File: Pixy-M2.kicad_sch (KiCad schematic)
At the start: 78 parts, among them J1 USB_C_Receptacle_USB2.0_14P, J10 SM09B-SRSS-TB, J11 SM06B-SRSS-TB, J4 SM06B-SRSS-TB, J5 SM06B-SRSS-TB, J6 SM06B-SRSS-TB, J7 SM06B-SRSS-TB, J8 SM06B-SRSS-TB, J9 SM06B-SRSS-TB, Q1 AO4407A, SW1 SW_Push, SW2 SW_Push, SW3 JS102011SAQN, U1 ESP32-S3-WROOM-1-N16, U2 USBLC6-2SC6, U3 AP63203WU, U4 DRV8231ADSG, U5 DRV8231ADSG

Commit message: layout: replace F1 with a fuse that breaks the pack's short-circuit current
The chosen pack (OVONIC 2S 450 mAh 100C, XT30) is estimated to put 200-400 A
into a dead short (8-15 mOhm/cell plus connectors, lead, fuse and copper; Ovonic
publishes no internal resistance). The 2920L300/15DR PPTC was rated to break
40 A. A lower-C pack was rejected to keep burst current for the motors, and the
451/453 NANO2 parts (300-400 A @ 32 VDC) sit inside the estimate.

F1 is now a Littelfuse 0885005.DR: 5 A fast-acting, 1500 A @ 125 VDC breaking,
11.9 mOhm. 5 A covers the ~2.4 A worst normal load (both motors at the 1.00 A
limit plus the buck) after the 25% derating. It is one-time: jams are handled
by the drivers' current limit and firmware stall detection. Symbol goes
Device:Polyfuse -> Device:Fuse (same pins); F2 stays a PPTC. Netlist diff:
only F1's value and footprint. ERC 0.

Board: new last routing stage, tools/autoroute/f1_fuse.py. The 16.1 x 7.3 mm
land pattern sits at (110.2, 100.7) between BT1 and Q1; its 7.76 mm courtyard
did not fit the 7.65 mm BT1-D6 gap, so BT1 moves 0.4 mm north (J6 still 2.6 mm
away; verify_placement.py: no underside clashes). /VBAT_RAW and /VBAT_FUSED
re-routed at 1.0 mm; no other net changed. D6's reference moved off F1 pad 2.
DRC: 0 violations, 0 unconnected, 0 parity. Aperture audit passes.

pololu_conn.py fixes found on the way, with J8/J9 copper unchanged:
_zone() uses pad extents rather than centres, and dangling() counts a track
end whose copper overlaps a pad or via as connected.

Co-Authored-By: Claude Opus 5.5 <noreply@anthropic.com>
Claude-Session: https://claude.ai/code/session_01MLrob72MX5PcwtzVMbc3bs
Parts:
- F1: value 3A 15V -> 5A 1500A@125VDC; footprint Fuse:Fuse_2920_7451Metric -> Fuse:Fuse_Littelfuse-NANO2-885; symbol Device:Polyfuse -> Device:Fuse; MPN 2920L300/15DR -> 0885005.DR
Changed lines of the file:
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@@
 	)
 	(symbol
-		(lib_id "Device:Polyfuse")
+		(lib_id "Device:Fuse")
 		(at 161.29 73.66 90)
 		(unit 1)
@@
 			)
 		)
-		(property "Value" "3A 15V"
+		(property "Value" "5A 1500A@125VDC"
 			(at 161.29 68.58 90)
 			(effects
@@
 			)
 		)
-		(property "Footprint" "Fuse:Fuse_2920_7451Metric"
+		(property "Footprint" "Fuse:Fuse_Littelfuse-NANO2-885"
 			(at 161.29 73.66 0)
 			(hide yes)
@@
 			)
 		)
-		(property "Datasheet" "https://www.littelfuse.com/assetdocs/2920l_datasheet_update.pdf?assetguid=f237e8c2-1ed9-4c13-a738-dbe0738b3d2c"
+		(property "Datasheet" "https://www.littelfuse.com/assetdocs/littelfuse-fuse-885-datasheet?assetguid=f4426cf6-2a53-41b3-b8da-211f7a44fad1"
 			(at 161.29 73.66 0)
 			(hide yes)
@@
 			)
 		)
-		(property "Description" "Battery PPTC: 3A hold / 5A trip at 20C, 15V, 40A maximum fault current. Provisional; verify motor/fan load and pack fault current."
+		(property "Description" "Battery fuse, one-time: Littelfuse 885 series 5A, breaks 1500A @ 125VDC. Sized for the pack short-circuit current (OVONIC 2S 450mAh 100C, est. 200-400A); the old 2920 PPTC was rated for 40A max fault. 200% opens in 2 min max; max normal load ~2.4A."
 			(at 161.29 73.66 0)
 			(hide yes)
@@
 			)
 		)
-		(property "MPN" "2920L300/15DR"
+		(property "MPN" "0885005.DR"
 			(at 161.29 73.66 0)
 			(hide yes)

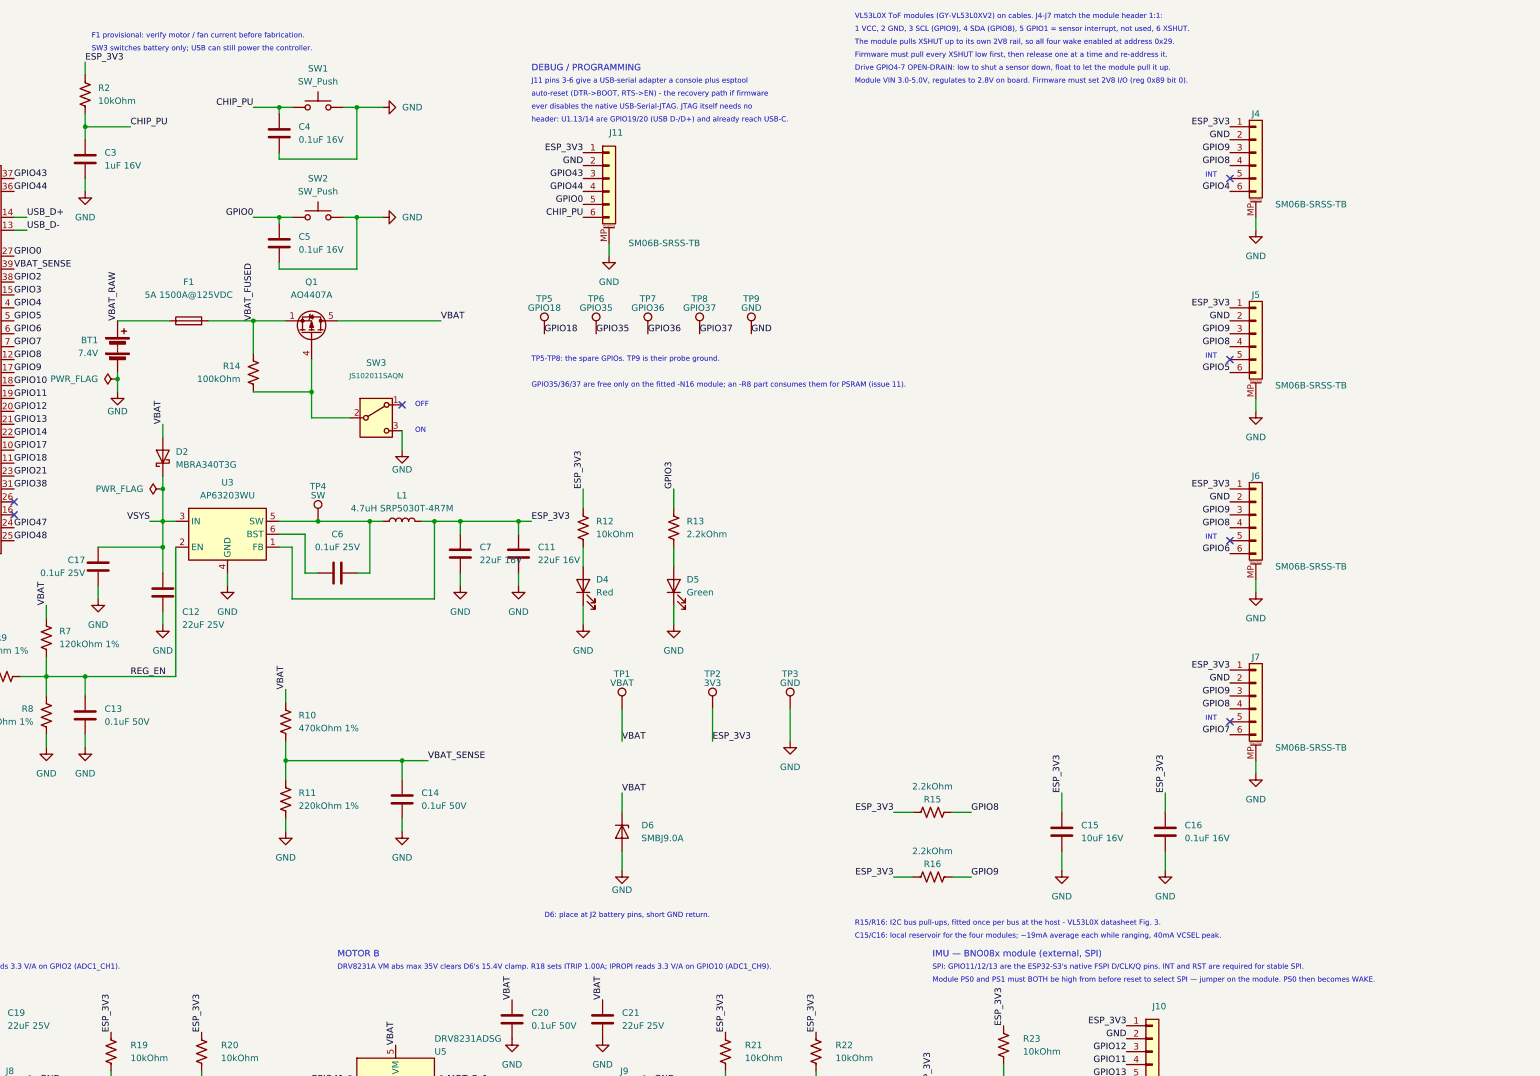
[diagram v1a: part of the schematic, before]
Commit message: schematic: correct three stale sheet notes
- F1 is no longer provisional: it is the 0885005.DR one-time fuse, sized
  to break the pack's short-circuit current, and there is no fan.
- D6 goes beside the motor drivers; J2 was deleted on 2026-09-20.
- The IMU note implied both PS0 and PS1 are module jumpers. Only PS1 is;
  PS0 is WAKE on GPIO17, held high by firmware while RST is pulsed.

Text only: the netlist is byte-identical and ERC is 0. The README's
schematic render is regenerated to match.

Co-Authored-By: Claude Opus 5.5 <noreply@anthropic.com>
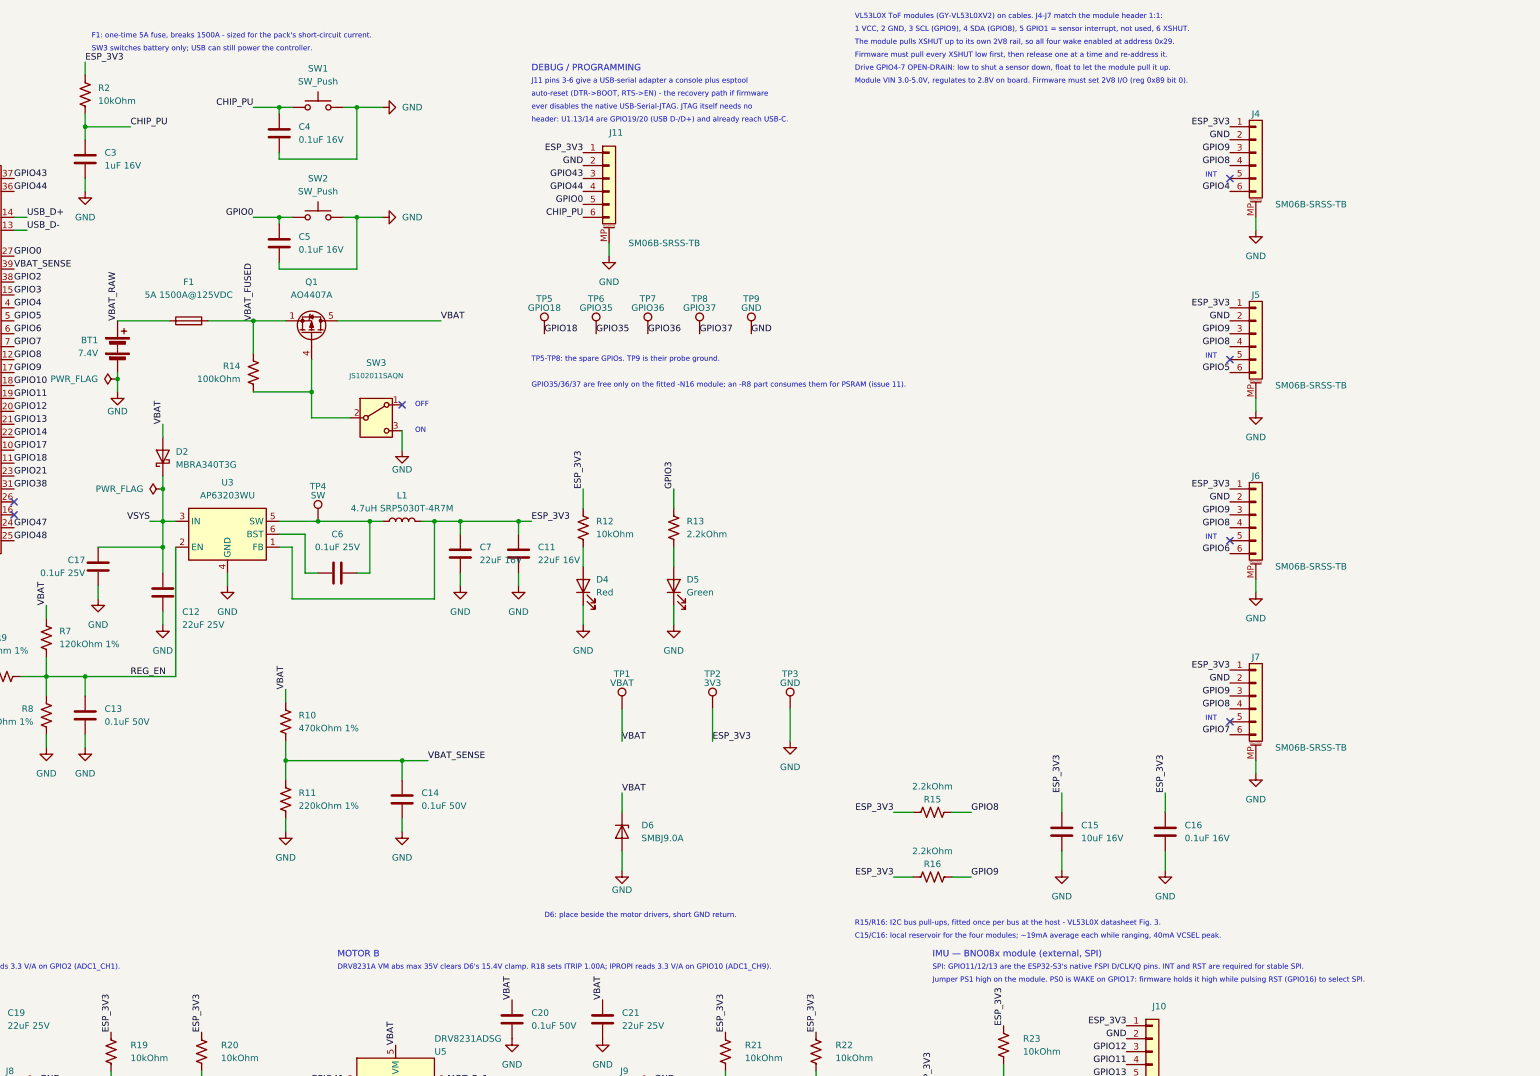
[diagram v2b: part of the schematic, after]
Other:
- note added: "D6: place beside the motor drivers, short GND return."
- note added: "F1: one-time 5A fuse, breaks 1500A - sized for the pack's short-circuit current."
- note added: "Jumper PS1 high on the module. PS0 is WAKE on GPIO17: firmware holds it high while pulsing RST (GPIO16) to select SPI."
- note removed: "D6: place at J2 battery pins, short GND return."
- note removed: "F1 provisional: verify motor / fan current before fabrication."
- note removed: "Module PS0 and PS1 must BOTH be high from before reset to select SPI — jumper on the module. PS0 then becomes WAKE."
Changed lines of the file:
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@@
 		)
 	)
-	(text "F1 provisional: verify motor / fan current before fabrication."
+	(text "F1: one-time 5A fuse, breaks 1500A - sized for the pack's short-circuit current."
 		(at 142.24 17.78 0)
 		(effects
@@
 		)
 	)
-	(text "D6: place at J2 battery pins, short GND return."
+	(text "D6: place beside the motor drivers, short GND return."
 		(at 231.14 190.5 0)
 		(effects
@@
 		)
 	)
-	(text "Module PS0 and PS1 must BOTH be high from before reset to select SPI — jumper on the module. PS0 then becomes WAKE."
+	(text "Jumper PS1 high on the module. PS0 is WAKE on GPIO17: firmware holds it high while pulsing RST (GPIO16) to select SPI."
 		(at 307.34 203.2 0)
 		(effects

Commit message: schematic: re-lay out the sheet into framed blocks
Layout only. Every wire-connected cluster moved rigidly into one of 13
dashed, titled frames in three rows: MCU, reset/boot, indicators/test
points, debug, battery sense, ToF; USB-C, battery input, 3V3 buck, UVLO;
motor A, motor B, IMU. The empty bottom band and right-centre of the A3
sheet are now used.

Two blocks were redrawn inside:
- USB: the CC resistors drop to GND without crossing D+/D-, the pair
  steps down to a lowered U2, and U2 takes VBUS by label.
- UVLO: the divider reaches U3.2 through its existing REG_EN label
  instead of a wire under the buck, so the blocks can sit apart.

Also fixed text overlaps: C1/C2, C7/C11, C8/R5 and C12. Long notes are
re-wrapped; their wording is unchanged.

Verified: netlist diff 0 differences (66 nets, 78 parts), ERC 0/0, PCB
DRC with schematic parity 0 violations / 0 unconnected / 0 parity. The
scripts are in tools/schematic, with netdiff.py for future edits.

Co-Authored-By: Claude Opus 5.5 <noreply@anthropic.com>
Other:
- note added: "3V3 BUCK — AP63203"
- note added: "BATTERY INPUT / POWER SWITCH"
- note added: "BATTERY SENSE"
- note added: "INDICATORS / TEST POINTS"
- note added: "MCU — ESP32-S3-WROOM-1-N16"
- note added: "RESET / BOOT"
- note added: "TOF WALL SENSORS — 4× VL53L0X"
- note added: "USB-C INPUT"
- note added: "UVLO — REGULATOR ENABLE"
- moved on the sheet: BT1, C1, C11, C12, C13, C14, C15, C16, C17, C18, C19, C2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

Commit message: U1: plug-in ESP32-S3-DevKitC-1-N8R8 on SMD sockets, same 66 x 100 mm board
Replace the soldered WROOM-1 module with an Espressif ESP32-S3-DevKitC-1-N8R8
(v1.1) on two 1x22 2.54 mm SMD female headers, and remove what the devkit
carries itself. The outline stays 66 x 100 mm for the diagonal runs.

Schematic (tools/schematic/devkit.py):
- U1 -> PCM_Espressif:ESP32-S3-DevKitC on Pixy-M2:ESP32-S3-DevKitC-1_SMD_Sockets;
  Value, Footprint, Datasheet and MPN changed together.
- 21 parts removed: the USB-C input (J1, U2, F2, R1, R5, R6, C8), the USB
  supply path (D1, D3, R9), reset/boot (R2, C3-C5, SW1, SW2), J11 and TP5-TP8.
- The AP63203 feeds the devkit's 3V3 pins; its 5V pin is unused.
- Encoder B OUT B moves from GPIO38 (the v1.1 RGB LED) to GPIO18.
- 13 no-connect flags on the pins the devkit uses itself. 59 nets, 57 parts,
  ERC 0/0.

Layout (tools/autoroute/devkit.py, new rework stage 20):
- U1 along the right edge, antenna over the rear edge, USB end to the front.
- The IMU moves into the 25 mm column beside the devkit (8.6 mm left of and
  7.5 mm behind the rotation centre). J10/C22 go behind it, J8/SW3 clear of
  it, J9 in front of the devkit, the LEDs to the rear-left corner and the
  sense chain against GPIO1.
- Rips and re-routes every affected net, keeping the hand-placed motor-corner,
  buck, FB and REG_EN copper. A* respects the custom clearance floors. The
  stage ends with KiCad-style dead-end pruning, removal of via-only GND stubs
  and one GND via per B.Cu pour island.
- Closes J1's outline notch and moves the antenna keep-out.
- Footprint generator: tools/autoroute/devkit_footprint.py.
- DRC 0 violations / 0 unconnected / 0 parity. Aperture audit passes with
  192 vias (254 on main). A full rework.py replay reproduces the board.
- Measurements are in layout/devkit/. Motor loops: A 26.4 mm², B 27.8 mm²
  (main 23.9 / 9.8, where B's opposite lobes nearly cancelled).

Rules: USB rules and netclass removed; Hole clearance 0.30 mm everywhere.
via_openings.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
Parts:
- removed C3: 1uF 16V, Capacitor_SMD:C_0603_1608Metric, symbol Device:C
- removed C4, C5: 0.1uF 16V, Capacitor_SMD:C_0603_1608Metric, symbol Device:C
- removed C8: 4.7nF 1kV, Capacitor_SMD:C_1206_3216Metric, symbol Device:C
- removed D1: MBRA340T3G, Diode_SMD:D_SMA, symbol Device:D_Schottky
- removed D3: BAT54W, Diode_SMD:D_SOD-123, symbol Device:D_Schottky
- removed F2: 500mA 15V, Fuse:Fuse_1812_4532Metric, symbol Device:Polyfuse
- removed J1: USB_C_Receptacle_USB2.0_14P, Connector_USB:USB_C_Receptacle_Amphenol_12401948E412A, symbol Connector:USB_C_Receptacle_USB2.0_14P
- removed J11: SM06B-SRSS-TB, Connector_JST:JST_SH_SM06B-SRSS-TB_1x06-1MP_P1.00mm_Horizontal, symbol Connector_Generic_MountingPin:Conn_01x06_MountingPin
- removed R1, R6: 5.1kOhm, Resistor_SMD:R_0805_2012Metric, symbol Device:R_US
- removed R2: 10kOhm, Resistor_SMD:R_0805_2012Metric, symbol Device:R_US
- removed R5: 1MOhm, Resistor_SMD:R_0805_2012Metric, symbol Device:R_US
- removed R9: 39kOhm 1%, Resistor_SMD:R_0805_2012Metric, symbol Device:R_US
- removed SW1, SW2: SW_Push, Button_Switch_SMD:SW_Push_1P1T_NO_E-Switch_TL3301NxxxxxG, symbol Switch:SW_Push
- removed TP5: GPIO18, TestPoint:TestPoint_Pad_D1.5mm, symbol Connector:TestPoint
- removed TP6: GPIO35, TestPoint:TestPoint_Pad_D1.5mm, symbol Connector:TestPoint
- removed TP7: GPIO36, TestPoint:TestPoint_Pad_D1.5mm, symbol Connector:TestPoint
- removed TP8: GPIO37, TestPoint:TestPoint_Pad_D1.5mm, symbol Connector:TestPoint
- removed U2: USBLC6-2SC6, Package_TO_SOT_SMD:SOT-23-6, symbol Power_Protection:USBLC6-2SC6
- U1: value ESP32-S3-WROOM-1-N16 -> ESP32-S3-DevKitC-1-N8R8; footprint Pixy-M2:ESP32-S3-WROOM-1_AntennaOverhang -> Pixy-M2:ESP32-S3-DevKitC-1_SMD_Sockets; symbol PCM_Espressif:ESP32-S3-WROOM-1 -> PCM_Espressif:ESP32-S3-DevKitC; MPN (none) -> ESP32-S3-DevKitC-1-N8R8
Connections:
- net GPIO0 is gone; now on net GPIO21: U1.27 (GPIO21)
- net GPIO35 is gone; now on net GPIO47: U1.28 (GPIO47)
- net GPIO36 is gone; now on net GPIO48: U1.29 (GPIO48)
- net GPIO43 is gone; now on net GPIO40: U1.37 (GPIO40/MTDO)
- net GPIO44 is gone; now on net GPIO39: U1.36 (GPIO39/MTCK)
- net USB_D- is gone; now on net GPIO3: U1.13 (GPIO3/ADC1_CH2)
- net ESP_3V3: now also U1.1 (3V3)
- net GND: now also U1.22 (GND), U1.23 (GND), U1.24 (GND), U1.44 (GND); no longer U1.1 (GND), U1.40 (GND), U1.41 (GND)
- net GPIO10: now also U1.16 (GPIO10/ADC1_CH9); no longer U1.18 (GPIO10/TOUCH10/ADC1_CH9/FSPICS0/FSPIIO4/SUBSPICS0)
- net GPIO11: now also U1.17 (GPIO11/ADC2_CH0); no longer U1.19 (GPIO11/TOUCH11/ADC2_CH0/FSPID/FSPIIO5/SUBSPID)
- net GPIO12: now also U1.18 (GPIO12/ADC2_CH1); no longer U1.20 (GPIO12/TOUCH12/ADC2_CH1/FSPICLK/FSPIIO6/SUBSPICLK)
- net GPIO13: now also U1.19 (GPIO13/ADC2_CH2); no longer U1.21 (GPIO13/TOUCH13/ADC2_CH2/FSPIQ/FSPIIO7/SUBSPIQ)
- net GPIO14: now also U1.20 (GPIO14/ADC2_CH3); no longer U1.22 (GPIO14/TOUCH14/ADC2_CH3/FSPIWP/FSPIDQS/SUBSPIWP)
- net GPIO18: now also J9.2 (Pin_2), R22.2
- net GPIO2: now also U1.40 (GPIO2/ADC1_CH1); no longer U1.38 (GPIO2/TOUCH2/ADC1_CH1)
- net GPIO21: no longer U1.23 (GPIO21)
- net GPIO3: no longer U1.15 (GPIO3/TOUCH3/ADC1_CH2)
- net GPIO39: no longer U1.32 (MTCK/GPIO39/CLK_OUT3/SUBSPICS1)
- net GPIO40: no longer U1.33 (MTDO/GPIO40/CLK_OUT2)
- net GPIO41: now also U1.38 (GPIO41/MTDI); no longer U1.34 (MTDI/GPIO41/CLK_OUT1)
- net GPIO42: now also U1.39 (GPIO42/MTMS); no longer U1.35 (MTMS/GPIO42)
- net GPIO47: no longer U1.24 (GPIO47/SPICLK_P/SUBSPICLK_P_DIFF)
- net GPIO48: no longer U1.25 (GPIO48/SPICLK_N/SUBSPICLK_N_DIFF)
- net GPIO9: now also U1.15 (GPIO9/ADC1_CH8); no longer U1.17 (GPIO9/TOUCH9/ADC1_CH8/FSPIHD/SUBSPIHD)
- net VBAT_SENSE: now also U1.41 (GPIO1/ADC1_CH0); no longer U1.39 (GPIO1/TOUCH1/ADC1_CH0)
- net CHIP_PU: no longer names the net of U1.3 (CHIP_PU)
- net GPIO37: no longer names the net of U1.30 (GPIO45)
- removed net GPIO38: J9.2 (Pin_2), R22.2, U1.31 (GPIO38/FSPIWP/SUBSPIWP)
- net USB_D+: no longer names the net of U1.14 (GPIO46)
- no-connect marks 7 -> 18
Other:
- note added: "DEVKITC-1 DAUGHTERBOARD — NOTES"
- note added: "GPIO19/20 (devkit USB), GPIO43/44 (devkit USB-UART), GPIO0 and CHIP_PU (devkit"
- note added: "Its own USB-UART and native-USB ports, BOOT/RESET buttons and CHIP_PU RC replace the"
- note added: "MCU — ESP32-S3-DevKitC-1-N8R8 (plug-in daughterboard)"
- note added: "No spare GPIOs remain."
- note added: "Power: the AP63203 feeds ESP_3V3 into the devkit's 3V3 pins; its 5V pin is unused."
- note added: "SW3 switches the battery only. USB reaches only the devkit's own LDO (see notes, left)."
- note added: "U1 is an ESP32-S3-DevKitC-1-N8R8 (v1.1) on two 1x22 2.54 mm SMD female headers."
- note added: "Unusable pins: GPIO35/36/37 (octal PSRAM on N8R8), GPIO38 (v1.1 RGB LED),"
- note added: "With USB plugged in, the devkit's SGM2212 LDO also drives 3V3. Neither source sinks"
- note added: "buttons), GPIO45/46 (strapping). Encoder B OUT B is on GPIO18 for that reason."
- note added: "current, so the two share the rail harmlessly, but Espressif calls the inputs"
- note added: "mutually exclusive. USB no longer reaches VSYS or REG_EN: the motors and the UVLO"
- note added: "removed USB-C input, J11 and SW1/SW2. Flash and debug through the devkit's USB ports."
- note added: "see only the pack, and the hardware UVLO now holds with USB attached."
- note removed: "DEBUG / PROGRAMMING"
- note removed: "GPIO35/36/37 are free only on the fitted -N16 module; an -R8 part consumes them for PSRAM (issue 11)."
- note removed: "J11 pins 3-6 give a USB-serial adapter a console plus esptool"
- note removed: "MCU — ESP32-S3-WROOM-1-N16"
- note removed: "RESET / BOOT"
- note removed: "SW3 switches battery only; USB can still power the controller."
- note removed: "TP5-TP8: the spare GPIOs. TP9 is their probe ground."
- note removed: "USB-C INPUT"
- note removed: "auto-reset (DTR->BOOT, RTS->EN) - the recovery path if firmware"
- note removed: "ever disables the native USB-Serial-JTAG. JTAG itself needs no"
- note removed: "header: U1.13/14 are GPIO19/20 (USB D-/D+) and already reach USB-C."
- moved on the sheet: TP9
